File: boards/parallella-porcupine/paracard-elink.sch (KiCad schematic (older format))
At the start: 1 part, among them P2 CONN\\SAMTEC\\BTH\\60

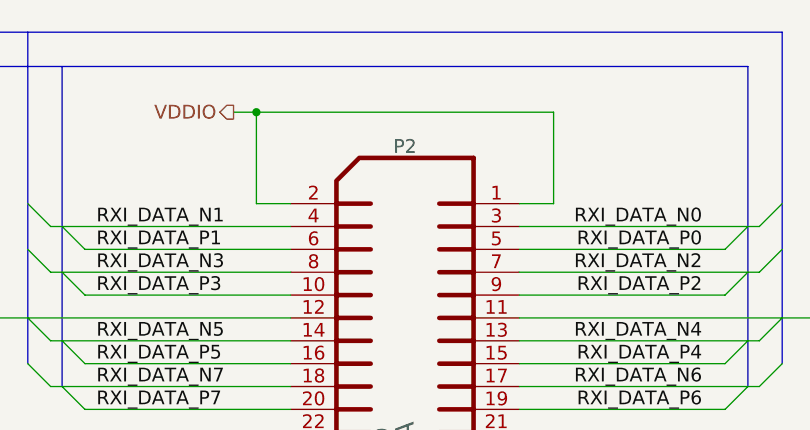
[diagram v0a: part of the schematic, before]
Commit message: Schematic is stable, PCB mostly routed.
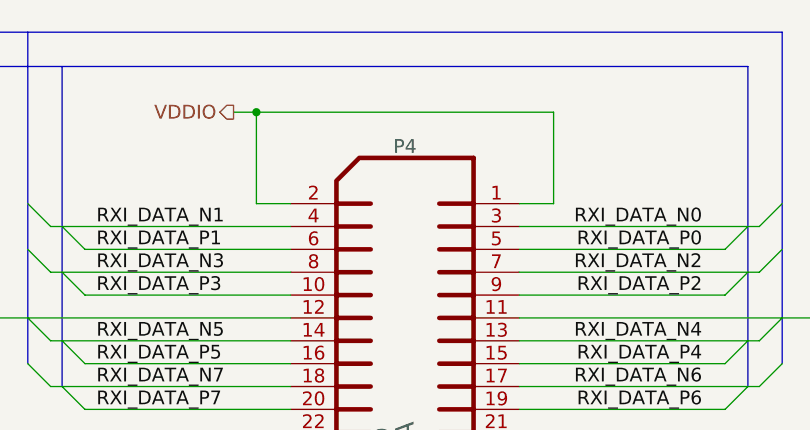
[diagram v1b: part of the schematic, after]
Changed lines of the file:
@@
 P 6500 7100
 AR Path="/5386858E/53875004" Ref="#PWR03"  Part="1"
-AR Path="/538F26B7/53875004" Ref="#PWR031"  Part="1"
-F 0 "#PWR03" H 6500 7100 30  0001 C CNN
+AR Path="/538F26B7/53875004" Ref="#PWR030"  Part="1"
+F 0 "#PWR030" H 6500 7100 30  0001 C CNN
 F 1 "GND" H 6500 7030 30  0001 C CNN
 F 2 "" H 6500 7100 60  0000 C CNN
@@
 P 10400 7100
 AR Path="/5386858E/53875018" Ref="#PWR04"  Part="1"
-AR Path="/538F26B7/53875018" Ref="#PWR032"  Part="1"
-F 0 "#PWR04" H 10400 7100 30  0001 C CNN
+AR Path="/538F26B7/53875018" Ref="#PWR031"  Part="1"
+F 0 "#PWR031" H 10400 7100 30  0001 C CNN
 F 1 "GND" H 10400 7030 30  0001 C CNN
 F 2 "" H 10400 7100 60  0000 C CNN
@@
 AR Path="/5386858E/53893761" Ref="P2"  Part="1"
 AR Path="/538F26B7/53893761" Ref="P4"  Part="1"
-F 0 "P2" H 8450 6550 60  0000 C CNN
+F 0 "P4" H 8450 6550 60  0000 C CNN
 F 1 "CONN\\SAMTEC\\BTH\\60" V 8350 4850 60  0000 C CNN
 F 2 "CONN_SAMTEC_BTH_60" V 8550 4850 60  0001 C CNN

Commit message: Completed design w/3-row XID/YID and various 4-pin IO connectors. Fixed page ordering, changed "Mfr" field to "Manufacturer" Will now re-do to combine all misc. functions onto a single 2xN connector.
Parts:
- P2: MFR Samtec -> (none); Manufacturer (none) -> Samtec
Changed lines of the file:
@@
 $Descr B 17000 11000
 encoding utf-8
-Sheet 9 10
+Sheet 5 10
 Title "Parallella Breakout Daughtercard"
 Date "09 May 2014"
@@
 TXO_DATA_N[0..7]
 $Comp
-L GND #PWR03
+L GND #PWR05
 U 1 1 53875004
 P 6500 7100
-AR Path="/5386858E/53875004" Ref="#PWR03"  Part="1"
-AR Path="/538F26B7/53875004" Ref="#PWR030"  Part="1"
-F 0 "#PWR030" H 6500 7100 30  0001 C CNN
+AR Path="/5386858E/53875004" Ref="#PWR05"  Part="1"
+AR Path="/538F26B7/53875004" Ref="#PWR07"  Part="1"
+F 0 "#PWR07" H 6500 7100 30  0001 C CNN
 F 1 "GND" H 6500 7030 30  0001 C CNN
 F 2 "" H 6500 7100 60  0000 C CNN
@@
 $EndComp
 $Comp
-L GND #PWR04
+L GND #PWR06
 U 1 1 53875018
 P 10400 7100
-AR Path="/5386858E/53875018" Ref="#PWR04"  Part="1"
-AR Path="/538F26B7/53875018" Ref="#PWR031"  Part="1"
-F 0 "#PWR031" H 10400 7100 30  0001 C CNN
+AR Path="/5386858E/53875018" Ref="#PWR06"  Part="1"
+AR Path="/538F26B7/53875018" Ref="#PWR08"  Part="1"
+F 0 "#PWR08" H 10400 7100 30  0001 C CNN
 F 1 "GND" H 10400 7030 30  0001 C CNN
 F 2 "" H 10400 7100 60  0000 C CNN
@@
 F 1 "CONN\\SAMTEC\\BTH\\60" V 8350 4850 60  0000 C CNN
 F 2 "CONN_SAMTEC_BTH_60" V 8550 4850 60  0001 C CNN
-F 3 "/mnt/windowsC/Adapteva/Fred-suppliers/Suppliers/www.samtec.com/BTH-XXX-XX-X-D-XX-MKT.pdf" H 8550 5750 60  0001 C CNN
+F 3 "" H 8550 5750 60  0001 C CNN
 F 4 "BTH-030-01-F-D-A" V 8450 4850 80  0000 C CNN "MFRPN"
-F 5 "Samtec" V 8450 3650 60  0000 C CNN "MFR"
+F 5 "Samtec" V 8450 3650 60  0000 C CNN "Manufacturer"
 	1    8450 4850
 	1    0    0    -1

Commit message: Ready for full review.
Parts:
- renumbered P2 to P3
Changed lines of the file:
@@
 $Descr B 17000 11000
 encoding utf-8
-Sheet 5 10
+Sheet 4 10
 Title "Parallella Breakout Daughtercard"
-Date "09 May 2014"
+Date "19 Jun 2014"
 Rev "*"
 Comp "Adapteva, Inc., 1666 Massachusetts Ave., Lexington, MA, 02420"
-Comment1 "Porcupin Top Level"
+Comment1 "Parallella eLink Connector"
 Comment2 ""
 Comment3 ""
@@
 AR Path="/5386858E/53875004" Ref="#PWR05"  Part="1"
 AR Path="/538F26B7/53875004" Ref="#PWR07"  Part="1"
-F 0 "#PWR07" H 6500 7100 30  0001 C CNN
+F 0 "#PWR05" H 6500 7100 30  0001 C CNN
 F 1 "GND" H 6500 7030 30  0001 C CNN
 F 2 "" H 6500 7100 60  0000 C CNN
@@
 AR Path="/5386858E/53875018" Ref="#PWR06"  Part="1"
 AR Path="/538F26B7/53875018" Ref="#PWR08"  Part="1"
-F 0 "#PWR08" H 10400 7100 30  0001 C CNN
+F 0 "#PWR06" H 10400 7100 30  0001 C CNN
 F 1 "GND" H 10400 7030 30  0001 C CNN
 F 2 "" H 10400 7100 60  0000 C CNN
@@
 	9100 3000 7700 3000
 $Comp
-L CONN\SAMTEC\BTH\60 P2
+L CONN\SAMTEC\BTH\60 P3
 U 1 1 53893761
 P 8450 4850
-AR Path="/5386858E/53893761" Ref="P2"  Part="1"
+AR Path="/5386858E/53893761" Ref="P3"  Part="1"
 AR Path="/538F26B7/53893761" Ref="P4"  Part="1"
-F 0 "P4" H 8450 6550 60  0000 C CNN
+F 0 "P3" H 8450 6550 60  0000 C CNN
 F 1 "CONN\\SAMTEC\\BTH\\60" V 8350 4850 60  0000 C CNN
 F 2 "CONN_SAMTEC_BTH_60" V 8550 4850 60  0001 C CNN

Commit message: Porcupine Version 2.
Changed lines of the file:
@@
 LIBS:valves
 LIBS:porcupine-cache
-EELAYER 24 0
+EELAYER 25 0
 EELAYER END
 $Descr B 17000 11000
 encoding utf-8
-Sheet 4 10
-Title "Parallella Breakout Daughtercard"
-Date "19 Jun 2014"
-Rev "*"
+Sheet 5 11
+Title "Parallella Breakout Daughtercard, Ver. 2"
+Date "17 feb 2015"
+Rev "A"
 Comp "Adapteva, Inc., 1666 Massachusetts Ave., Lexington, MA, 02420"
-Comment1 "Parallella eLink Connector"
+Comment1 "Porcupine Top Level"
 Comment2 ""
 Comment3 ""
@@
 AR Path="/5386858E/53875004" Ref="#PWR05"  Part="1"
 AR Path="/538F26B7/53875004" Ref="#PWR07"  Part="1"
-F 0 "#PWR05" H 6500 7100 30  0001 C CNN
+F 0 "#PWR07" H 6500 7100 30  0001 C CNN
 F 1 "GND" H 6500 7030 30  0001 C CNN
 F 2 "" H 6500 7100 60  0000 C CNN
@@
 AR Path="/5386858E/53875018" Ref="#PWR06"  Part="1"
 AR Path="/538F26B7/53875018" Ref="#PWR08"  Part="1"
-F 0 "#PWR06" H 10400 7100 30  0001 C CNN
+F 0 "#PWR08" H 10400 7100 30  0001 C CNN
 F 1 "GND" H 10400 7030 30  0001 C CNN
 F 2 "" H 10400 7100 60  0000 C CNN
@@
 AR Path="/5386858E/53893761" Ref="P3"  Part="1"
 AR Path="/538F26B7/53893761" Ref="P4"  Part="1"
-F 0 "P3" H 8450 6550 60  0000 C CNN
+F 0 "P4" H 8450 6550 60  0000 C CNN
 F 1 "CONN\\SAMTEC\\BTH\\60" V 8350 4850 60  0000 C CNN
 F 2 "CONN_SAMTEC_BTH_60" V 8550 4850 60  0001 C CNN
